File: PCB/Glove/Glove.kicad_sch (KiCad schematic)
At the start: 36 parts, among them J1 JST-PH-SM4-TB, J2 USB-C-Socket-V, J3 Wago, J4 Reset, J5 BTN, J7 TC2030-USB-NL-DS, Q1 CJ2301, Q3 CJ2301, U1 ESP32-S3-MINI-1, U3 TP4054, U4 ME6211C33M5G-N

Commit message: Ready to track
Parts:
- removed D24: ~, RevK:DFN1006-2L, symbol RevK:ES05D1MC10
- added R6: 10K, RevK:R_0402, symbol Device:R
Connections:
- net +3.3V: now also J3.3 (Pin_3), R6.1
- net BTN: now also R6.2
- net D-: now also U1.23 (GPIO19)
- net VBAT: no longer J3.3 (Pin_3)
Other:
- moved on the sheet: D1, J3

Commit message: Ready to order
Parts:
- J1: Rotation Offset (none) -> 180
- U4: JLCPCB Rotation Offset -90 -> (none); Rotation Offset (none) -> 90
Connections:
- net BTN: now also U1.6 (GPIO2); no longer U1.5 (GPIO1)
- net CHARGING: now also U1.21 (GPIO17); no longer U1.7 (GPIO3)
- net LED: now also U1.15 (GPIO11); no longer U1.8 (GPIO4)
- net RGB: now also U1.9 (GPIO5); no longer U1.6 (GPIO2)
- net USB: now also U1.22 (GPIO18); no longer U1.10 (GPIO6)
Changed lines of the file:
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@@
 	)
 	(no_connect
-		(at 42.545 45.72)
+		(at 42.545 43.18)
 	)
 	(no_connect
@@
 	)
 	(no_connect
-		(at 42.545 78.74)
+		(at 42.545 40.64)
 	)
 	(no_connect
@@
 	)
 	(no_connect
-		(at 42.545 60.96)
+		(at 42.545 35.56)
 	)
 	(no_connect
@@
 	)
 	(no_connect
-		(at 42.545 76.2)
+		(at 42.545 48.26)
 	)
 	(wire
@@
 	(wire
 		(pts
-			(xy 107.95 100.33) (xy 111.76 100.33)
-		)
-		(stroke
-			(width 0)
-			(type default)
-		)
-	)
-	(wire
-		(pts
 			(xy 269.875 65.405) (xy 276.225 65.405)
 		)
@@
 	(global_label "CHARGING"
 		(shape input)
-		(at 42.545 40.64 180)
+		(at 42.545 76.2 180)
 		(fields_autoplaced yes)
 		(effects
@@
 		)
 		(property "Intersheetrefs" "${INTERSHEET_REFS}"
-			(at 30.7796 40.64 0)
+			(at 30.7796 76.2 0)
 			(effects
 				(font
@@
 	(global_label "LED"
 		(shape output)
-		(at 42.545 43.18 180)
+		(at 42.545 60.96 180)
 		(fields_autoplaced yes)
 		(effects
@@
 		)
 		(property "Intersheetrefs" "${INTERSHEET_REFS}"
-			(at 36.7669 43.18 0)
+			(at 36.7669 60.96 0)
 			(effects
 				(font
@@
 	(global_label "BTN"
 		(shape input)
-		(at 42.545 35.56 180)
+		(at 42.545 38.1 180)
 		(fields_autoplaced yes)
 		(effects
@@
 		)
 		(property "Intersheetrefs" "${INTERSHEET_REFS}"
-			(at 36.6459 35.56 0)
+			(at 36.6459 38.1 0)
 			(effects
 				(font
@@
 	(global_label "USB"
 		(shape input)
-		(at 42.545 48.26 180)
+		(at 42.545 78.74 180)
 		(fields_autoplaced yes)
 		(effects
@@
 		)
 		(property "Intersheetrefs" "${INTERSHEET_REFS}"
-			(at 36.404 48.26 0)
+			(at 36.404 78.74 0)
 			(effects
 				(font
@@
 	(global_label "RGB"
 		(shape output)
-		(at 42.545 38.1 180)
+		(at 42.545 45.72 180)
 		(fields_autoplaced yes)
 		(effects
@@
 		)
 		(property "Intersheetrefs" "${INTERSHEET_REFS}"
-			(at 36.404 38.1 0)
+			(at 36.404 45.72 0)
 			(effects
 				(font
@@
 			)
 		)
-		(property "JLCPCB Rotation Offset" "-90"
+		(property "Rotation Offset" "90"
 			(at 187.325 32.385 0)
 			(effects
@@
 	(symbol
 		(lib_id "power:GND")
-		(at 107.95 100.33 270)
+		(at 111.76 100.33 0)
 		(unit 1)
 		(exclude_from_sim no)
@@
 		(fields_autoplaced yes)
 		(property "Reference" "#PWR03"
-			(at 101.6 100.33 0)
+			(at 111.76 106.68 0)
 			(effects
 				(font
@@
 		)
 		(property "Value" "GND"
-			(at 104.7751 100.33 90)
+			(at 113.665 101.6 0)
 			(effects
 				(font
 					(size 1.27 1.27)
 				)
-				(justify right)
+				(justify left)
 			)
 		)
 		(property "Footprint" ""
-			(at 107.95 100.33 0)
+			(at 111.76 100.33 0)
 			(effects
 				(font
@@
 		)
 		(property "Datasheet" ""
-			(at 107.95 100.33 0)
+			(at 111.76 100.33 0)
 			(effects
 				(font
@@
 		)
 		(property "Description" "Power symbol creates a global label with name \"GND\" , ground"
-			(at 107.95 100.33 0)
+			(at 111.76 100.33 0)
 			(effects
 				(font
@@
 			(at 137.16 67.945 0)
 			(effects
+				(font
+					(size 1.27 1.27)
+				)
+				(hide yes)
+			)
+		)
+		(property "Rotation Offset" "180"
+			(at 137.16 67.945 0)
+			(effects

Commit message: PCB Update
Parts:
- C1, C26: LCSC Part # C141660 -> (none); MPN (none) -> C141660
- C2: JLCPCB Rotation Offset 180 -> (none); LCSC Part # C106188 -> (none); MPN (none) -> C106188
- D1, D20, D3: LCSC Part # C5137770 -> (none); MPN (none) -> C5137770
- D2: LCSC Part  C5204746 -> (none); MPN (none) -> C5204746
- D4: LCSC Part # C5349953 -> (none); MPN (none) -> C5349953
- J1: LCSC Part # C295747 -> (none); MPN (none) -> C295747; Rotation Offset 180 -> (none)
- J2: LCSC Part # C709357 -> (none); MPN (none) -> C709357
- J3: LCSC Part # C2765056 -> (none); MPN (none) -> C2765056
- J5: LCSC Part # C2765055 -> (none); MPN (none) -> C2765055
- Q1, Q3: JLCPCB Rotation Offset 180 -> (none); LCSC Part # C5224170 -> (none); MPN (none) -> C5224170
- R11, R7, R8, R9: LCSC Part # C5139597 -> (none); MPN (none) -> C5139597
- U1: LCSC Part # C3013941 -> (none); MPN (none) -> C3013941
- U3: JLCPCB Rotation Offset 180 -> (none); LCSC Part # C668215 -> (none); MPN (none) -> C668215
- U4: LCSC Part # C82942 -> (none); MPN (none) -> C82942; Rotation Offset 90 -> (none)
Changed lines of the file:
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@@
 	)
 	(junction
-		(at 222.25 40.005)
-		(diameter 0)
-		(color 0 0 0 0)
-	)
-	(junction
 		(at 127.635 67.945)
 		(diameter 0)
@@
 	)
 	(junction
+		(at 222.25 40.005)
+		(diameter 0)
+		(color 0 0 0 0)
+	)
+	(junction
 		(at 86.36 89.535)
 		(diameter 0)
@@
 			)
 		)
-		(property "LCSC Part #" "C141660"
+		(property "MPN" "C141660"
 			(at 198.12 37.465 0)
 			(effects
@@
 			)
 		)
-		(property "LCSC Part #" "C82942"
-			(at 187.325 32.385 0)
-			(effects
-				(font
-					(size 1.27 1.27)
-				)
-				(hide yes)
-			)
-		)
-		(property "Rotation Offset" "90"
+		(property "MPN" "C82942"
 			(at 187.325 32.385 0)
 			(effects
@@
 			)
 		)
-		(property "LCSC Part #" "C5139597"
+		(property "MPN" "C5139597"
 			(at 219.075 87.63 90)
 			(effects
@@
 			)
 		)
-		(property "LCSC Part #" "C5139597"
+		(property "MPN" "C5139597"
 			(at 222.25 43.815 90)
 			(effects
@@
 			)
 		)
-		(property "LCSC Part #" "C5349953"
+		(property "MPN" "C5349953"
 			(at 113.03 85.09 0)
 			(effects
@@
 			)
 		)
-		(property "LCSC Part #" "C3013941"
+		(property "MPN" "C3013941"
 			(at 57.785 94.615 0)
 			(effects
@@
 			)
 		)
-		(property "LCSC Part #" "C709357"
+		(property "MPN" "C709357"
 			(at 241.935 80.645 0)
 			(effects
@@
 			)
 		)
-		(property "LCSC Part #" "C2765056"
+		(property "MPN" "C2765056"
 			(at 172.085 59.69 0)
 			(effects
@@
 			)
 		)
-		(property "LCSC Part #" "C2765055"
+		(property "MPN" "C2765055"
 			(at 182.88 88.265 0)
 			(effects
@@
 			)
 		)
-		(property "LCSC Part " "C5204746"
+		(property "MPN" "C5204746"
 			(at 172.72 37.465 0)
 			(effects
@@
 			)
 		)
-		(property "LCSC Part #" "C5224170"
-			(at 227.33 40.005 90)
-			(effects
-				(font
-					(size 1.27 1.27)
-				)
-				(hide yes)
-			)
-		)
-		(property "JLCPCB Rotation Offset" "180"
+		(property "MPN" "C5224170"
 			(at 227.33 40.005 90)
 			(effects
@@
 			)
 		)
-		(property "LCSC Part #" "C5137770"
+		(property "MPN" "C5137770"
 			(at 173.99 60.325 0)
 			(effects
@@
 			)
 		)
-		(property "LCSC Part #" "C106188"
-			(at 57.15 20.32 0)
-			(effects
-				(font
-					(size 1.27 1.27)
-				)
-				(hide yes)
-			)
-		)
-		(property "JLCPCB Rotation Offset" "180"
+		(property "MPN" "C106188"
 			(at 57.15 20.32 0)
 			(effects
@@
 			)
 		)
-		(property "LCSC Part #" "C668215"
+		(property "MPN" "C668215"
 			(at 121.92 29.845 0)
 			(effects
@@
 			)
 		)
-		(property "JLCPCB Rotation Offset" "180"
-			(at 119.38 27.94 0)
-			(effects
-				(font
-					(size 1.27 1.27)
-				)
-				(hide yes)
-			)
-		)
 		(pin "1"
 		)
@@
 			)
 		)
-		(property "LCSC Part #" "C5137770"
+		(property "MPN" "C5137770"
 			(at 166.37 89.535 0)
 			(effects
@@
 			)
 		)
-		(property "LCSC Part #" "C5137770"
+		(property "MPN" "C5137770"
 			(at 130.81 64.135 0)
 			(effects
@@
 			)
 		)
-		(property "LCSC Part #" "C5139597"
+		(property "MPN" "C5139597"
 			(at 219.075 80.01 90)
 			(effects
@@
 			)
 		)
-		(property "LCSC Part #" "C5139597"
+		(property "MPN" "C5139597"
 			(at 219.075 72.39 90)
 			(effects
@@
 			)
 		)
-		(property "LCSC Part #" "C5224170"
-			(at 163.83 32.385 90)
-			(effects
-				(font
-					(size 1.27 1.27)
-				)
-				(hide yes)
-			)
-		)
-		(property "JLCPCB Rotation Offset" "180"
+		(property "MPN" "C5224170"
 			(at 163.83 32.385 90)
 			(effects
@@
 			)
 		)
-		(property "LCSC Part #" "C141660"
+		(property "MPN" "C141660"
 			(at 269.875 61.595 90)
 			(effects
@@
 			)
 		)
-		(property "LCSC Part #" "C295747"
-			(at 137.16 67.945 0)
-			(effects
-				(font
-					(size 1.27 1.27)
-				)
-				(hide yes)
-			)
-		)
-		(property "Rotation Offset" "180"
+		(property "MPN" "C295747"
 			(at 137.16 67.945 0)
 			(effects

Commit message: Tidy
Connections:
- net D-: now also J7.2 (NC), J7.6 (NC)
- net GND: no longer J7.6 (GND)
- net VBUS: no longer J7.2 (VBUS)
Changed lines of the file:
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@@
 			)
 		)
-		(property "Datasheet" " ~"
+		(property "Datasheet" "~"
 			(at 97.79 41.91 0)
 			(effects

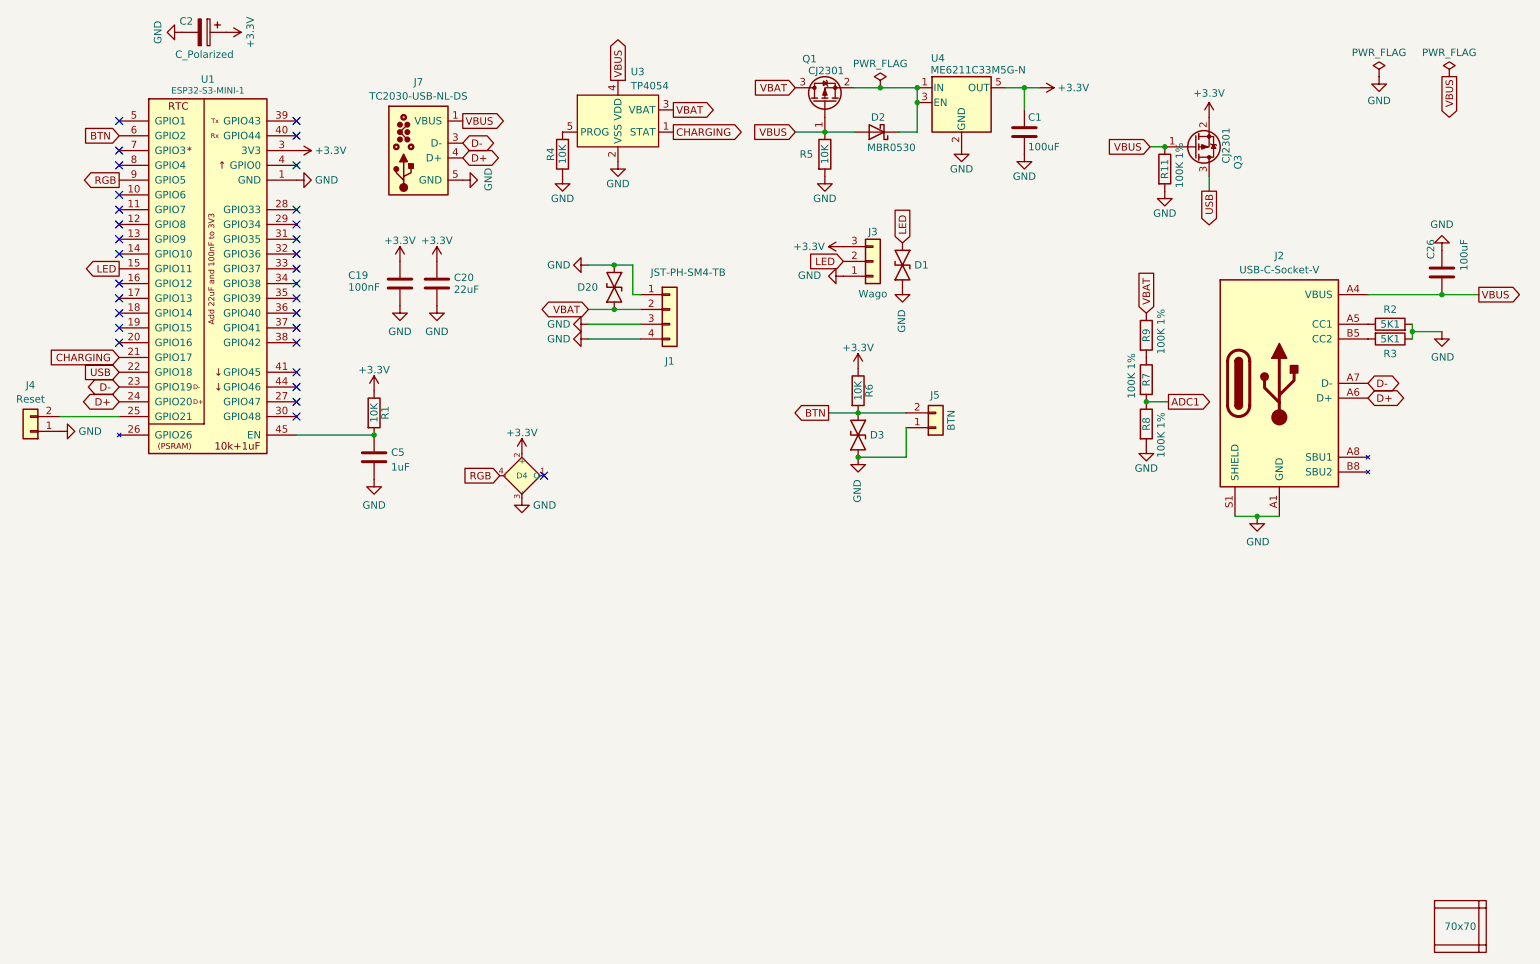
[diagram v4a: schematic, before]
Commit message: Added ADC and PWR
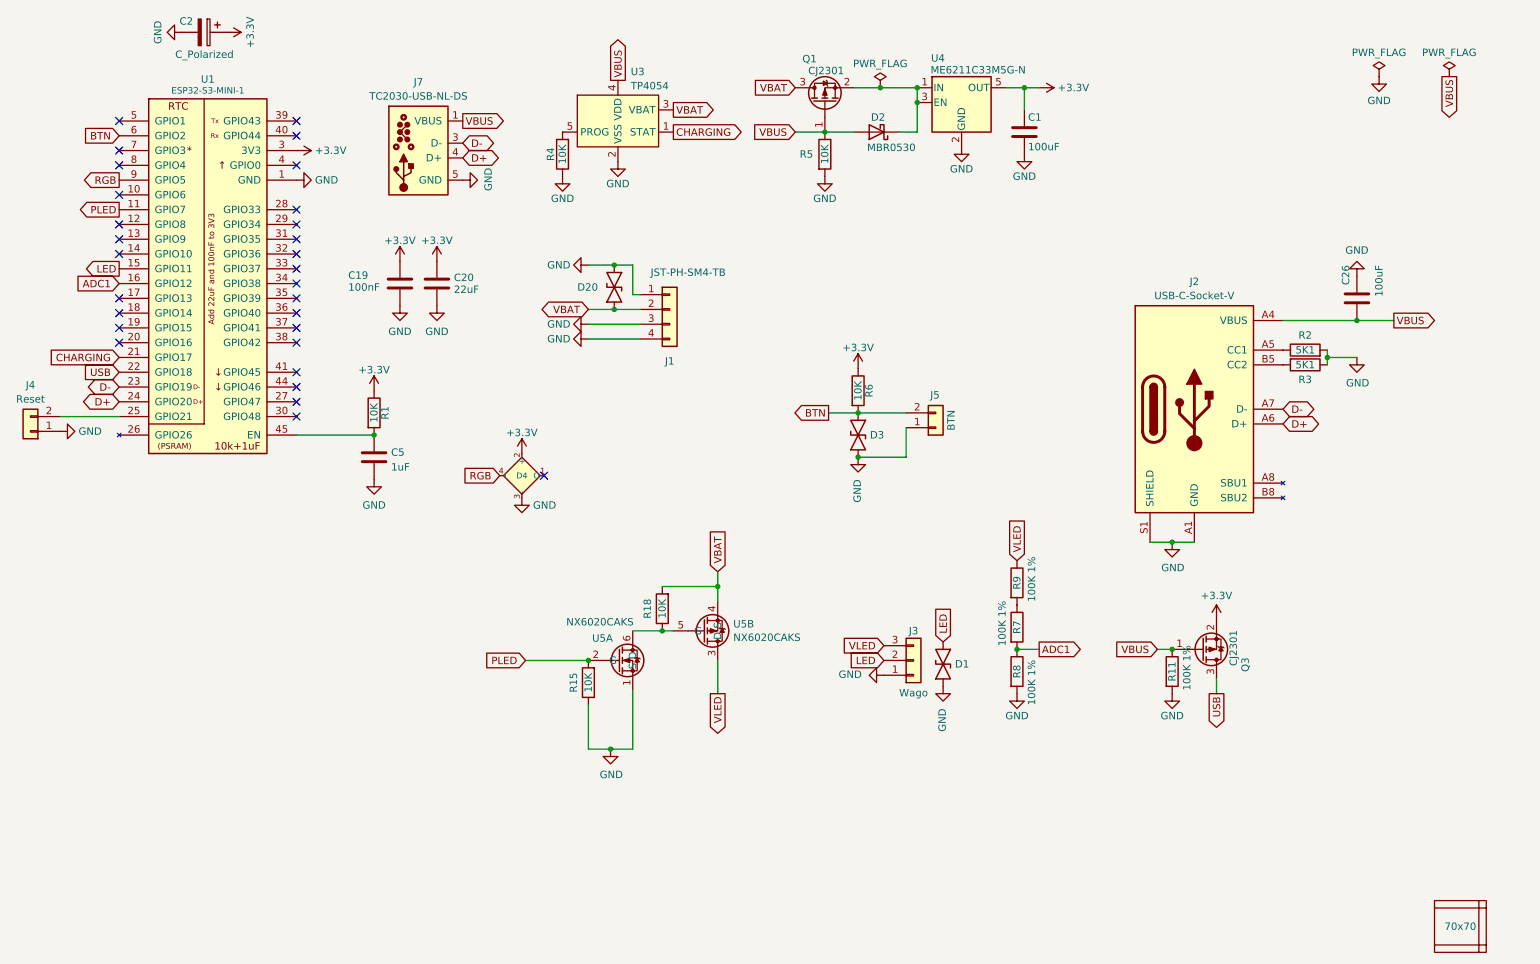
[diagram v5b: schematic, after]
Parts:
- added R15, R18: 10K, RevK:R_0402, symbol Device:R
- added U5: NX6020CAKS, RevK:SOT-363_SC-70-6, symbol RevK:NX6020CAKS
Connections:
- net +3.3V: no longer J3.3 (Pin_3)
- net ADC1: now also U1.16 (GPIO12)
- net GND: now also R15.1, U5.1 (S)
- net VBAT: now also R18.2, U5.4 (S); no longer R9.1
- net PLED: now reaches U1.11 (GPIO7)
- net PLED: now also R15.2, U5.2 (G)
- new net: R18.1, U5.5 (G), U5.6 (D)
- new net VLED: J3.3 (Pin_3), R9.1, U5.3 (D)
- no-connect marks 31 -> 29
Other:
- moved on the sheet: C26, D1, J2, J3, Q3, R11, R2, R3, R7, R8, R9
